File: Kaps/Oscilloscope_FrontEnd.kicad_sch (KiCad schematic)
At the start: 92 parts, among them J10 T_pwm, J11 T_buf, J12 T_buf, J13 ADC2, J14 ADC1, J15 +3.3VA, J16 +3.3VA, J3 T_att, J4 T_att, J5 T_acdc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

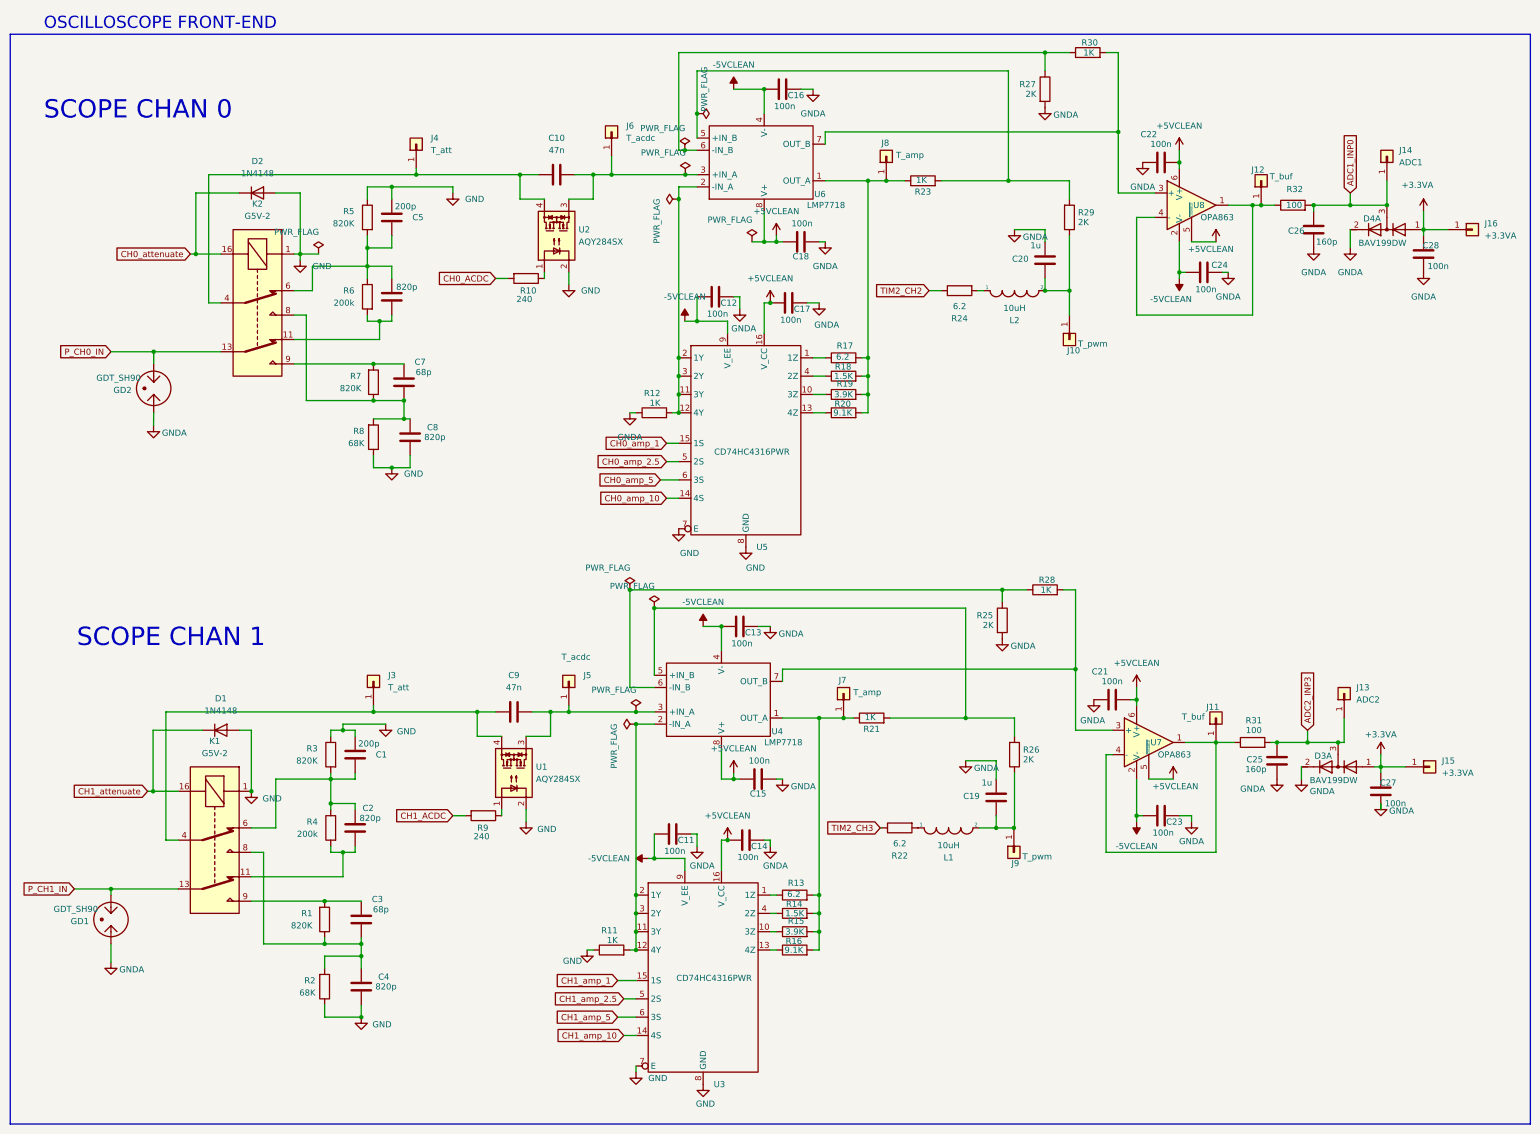
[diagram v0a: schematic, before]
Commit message: fixed grounds for several components and fix 5V clean
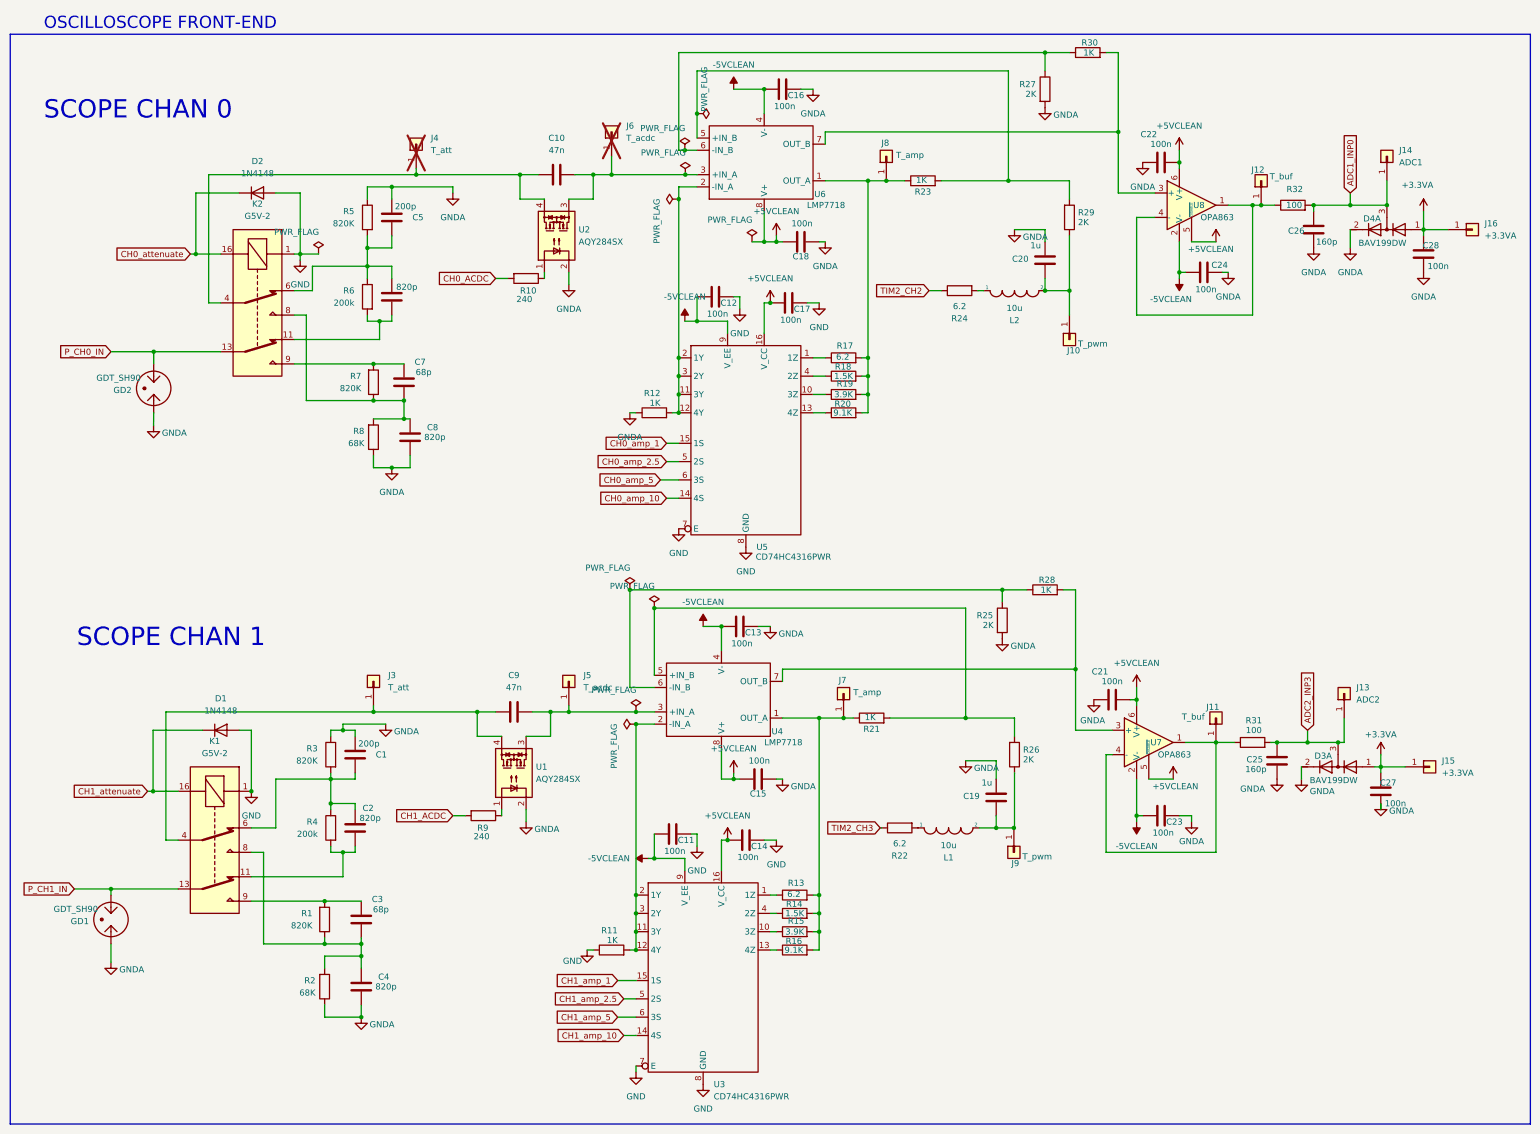
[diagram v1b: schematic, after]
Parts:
- J4, J6: now not fitted
- L1, L2: value 10uH -> 10u
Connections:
- net GND: now also C11.2, C12.2, C14.2, C17.2; no longer C1.1, C4.2, C5.1, C8.2, R2.1, R3.1, R5.1, R8.1, U1.2, U2.2
- net GNDA: now also C1.1, C4.2, C5.1, C8.2, R2.1, R3.1, R5.1, R8.1, U1.2, U2.2; no longer C11.2, C12.2, C14.2, C17.2
